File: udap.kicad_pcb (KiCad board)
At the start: 2 copper layers, 25 x 10 mm, 25 parts, among them J201 Conn_02x04_Counter_Clockwise, P1 USB_C_Plug, U2 MIC5245-3.3YM5, U201 NUF6401MNT1, U202 STM32F042F6Px, U4 NUF2042XV6T1G

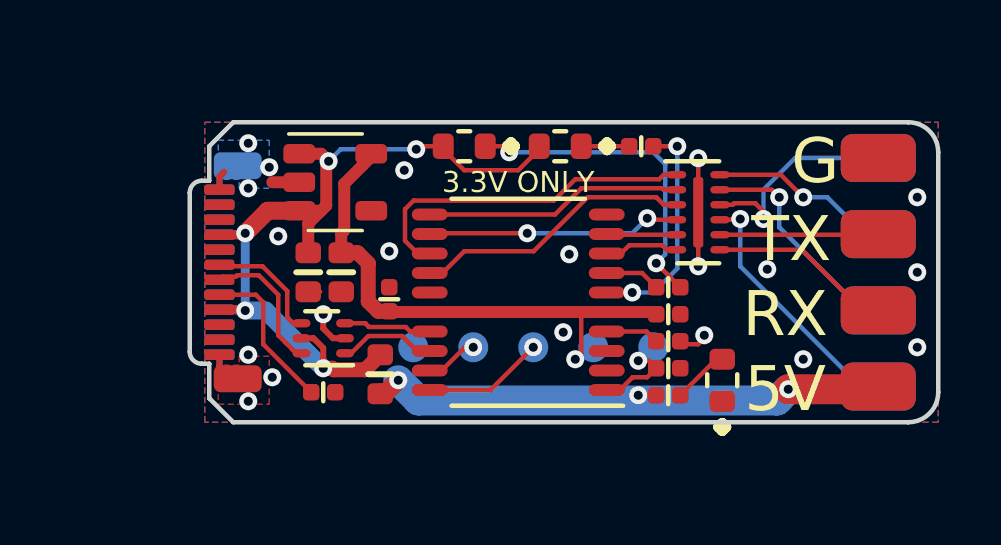
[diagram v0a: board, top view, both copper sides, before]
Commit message: USB-A version
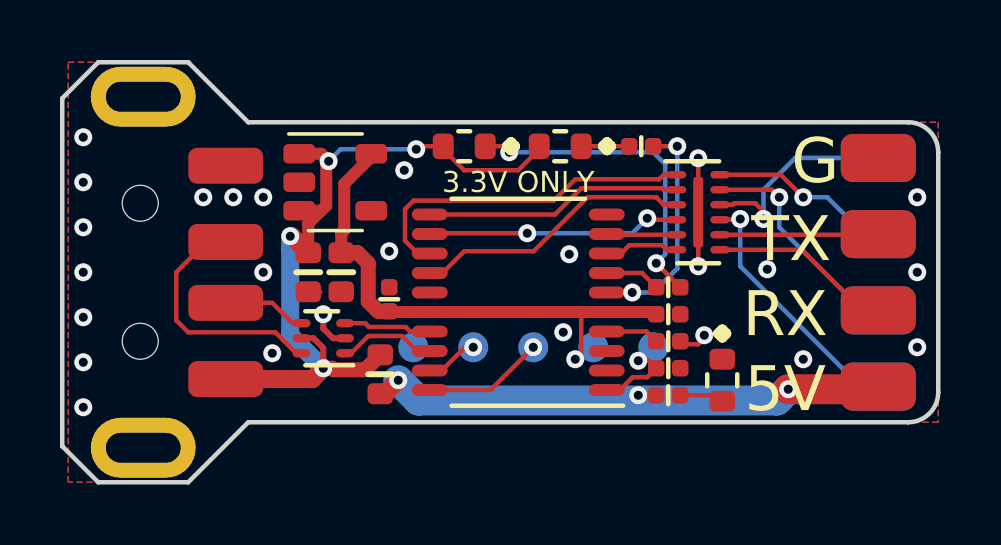
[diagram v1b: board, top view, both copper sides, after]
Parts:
- removed P1: USB_C_Plug, usb:USB_C_Plug_Molex_1054440001
- removed R3: 5.1k, passive:R_0402
- added P101: USB_A, usb:USB_A_1001-011-01101, F.Cu at (90.0, 106.0)
- turned D2 to 270 degrees
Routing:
- net Net-(P1-PadA5): track 5.23 -> 0.00 mm
- net GND: track 11.3 -> 6.17 mm, vias 20 -> 25
- net /DP: track 4.67 -> 8.30 mm
- net +5V: track 28.1 -> 25.6 mm, vias 5 -> 4
- net /DM: track 4.05 -> 2.81 mm
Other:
- board size 25 x 10 mm -> 29.2 x 14 mm
